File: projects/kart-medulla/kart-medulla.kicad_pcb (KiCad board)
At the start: 2 copper layers, 68 x 60 mm, 57 parts, among them CN1 1990012, CN2 1990012, CN3 1990012, CN4 1990012, CN5 1990012, CN6 1990012, CN7 1990012, CN8 1990012, Q3 IRLZ44NPBF, Q4 BSS123_C5184436, U1 LM358DR, U13 MCP4922-E/SL, U14 MAX4660EUA+T, U19 L7805CDT_C20611927, U23 SSW-122-01-T-D, U24 SSW-122-01-T-S, U25 PCF8574T/3,518, U5 SN74LVC3G17DCTR

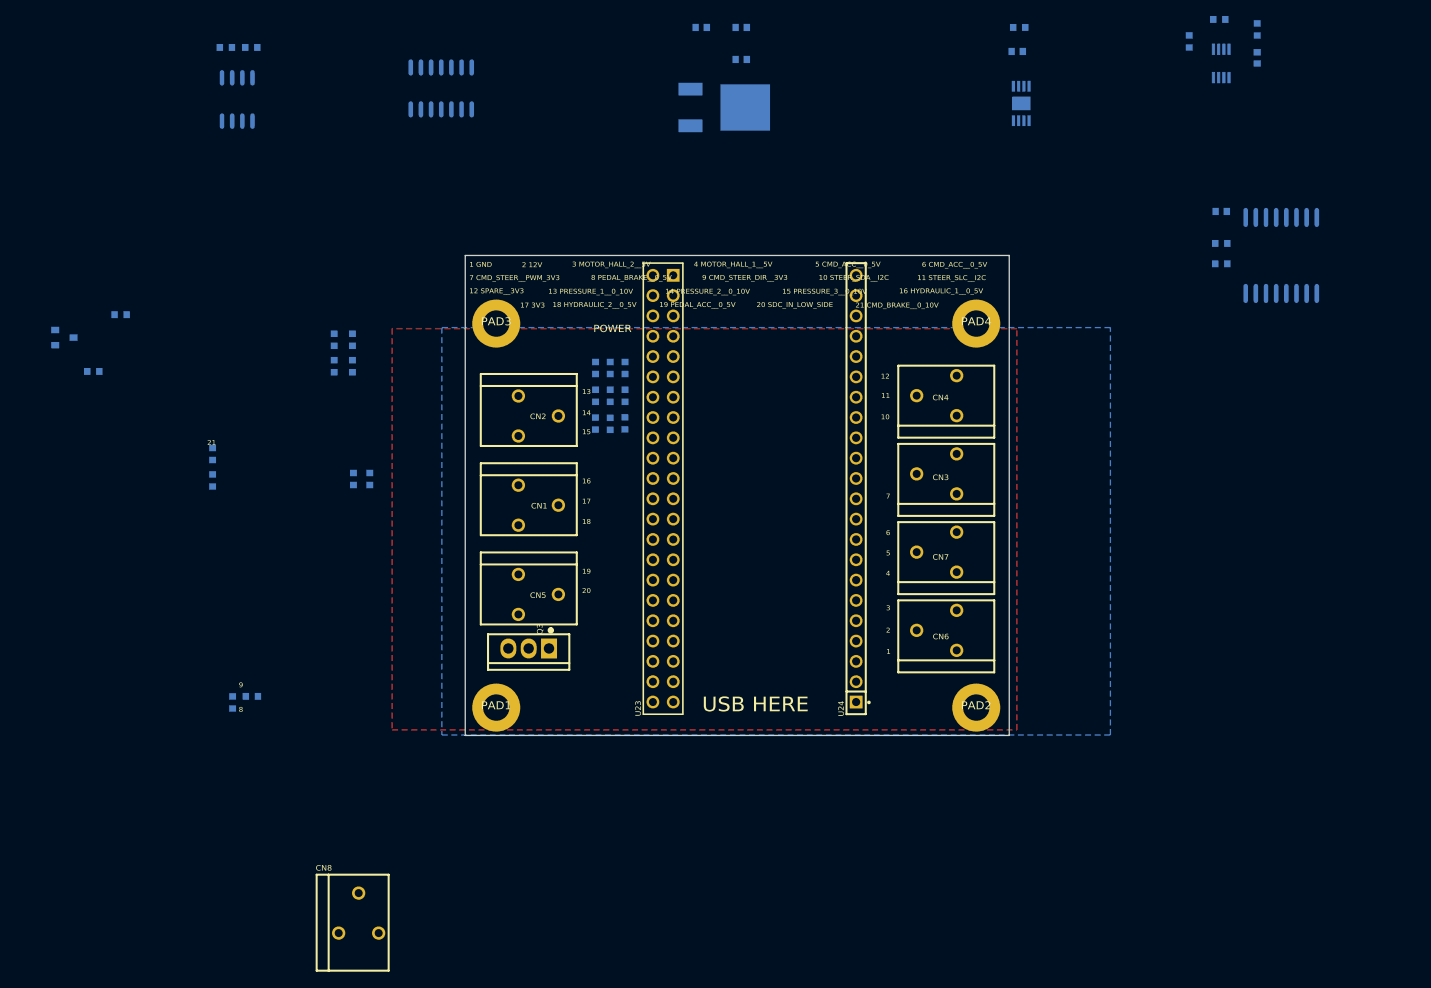
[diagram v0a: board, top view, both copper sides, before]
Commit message: kart-medulla: PCB↔schematic resync + agent workflow rules
PCB sync (the original goal — get ratsnest/Nets count right):
- Update PCB from Schematic with "Re-link footprints by reference"
  to repair empty symbol associations on every PCB footprint. Brings
  net count from 34 → ~80, ratsnest now populates correctly.
- Adds CN9, CN10 footprints that existed in schematic but not PCB.
- Footprint library names normalized to kart-medulla:* prefix.
- U23/U24 ESP32 header locks preserved (lock warnings benign).

Schematic cleanup:
- Delete stray kart-medulla:GND symbol with hidden Reference "U02"
  at (125.73, 311.15) — was buried under a standard power:GND at the
  same junction (redundant duplicate, no connectivity loss; ERC clean
  at that coord post-delete).

Agent workflow (addresses recurring failures in error-log):
- .agents/kicad-workflow.md — two-modes rule (read-only MCP vs
  direct-edit-with-KiCad-closed). KiCad has no schematic IPC API as
  of v10, so every schematic MCP server hand-rolls S-expression edits;
  mixing MCP writes with file edits silently clobbers. Default to
  Mode A (read-only MCP).
- scripts/guard-kicad-write.sh — pgrep preflight for KiCad GUI and
  kicad-mcp-pro before any agent-driven write.
- AGENTS.md — pointer to the workflow doc.
- .agents/kicad10-ui.md (user-authored) — verified UI cheat-sheet to
  stop the recurring "invented menu path" mistakes.
- tasks.md — buzzer circuit added to TODO.

Lessons logged in .agents/error-log.md and .agents/history.md:
- Don't grade edit options "safe vs risky" without grepping coords/nets first.
- Stacked symbols + Cmd+F selecting a Field-not-Symbol confusion in KiCad GUI.
- Don't pivot to unrelated TODOs while a workstream is in flight.
- kicad-sch-api round-trip is not format-preserving; not safe for writes.
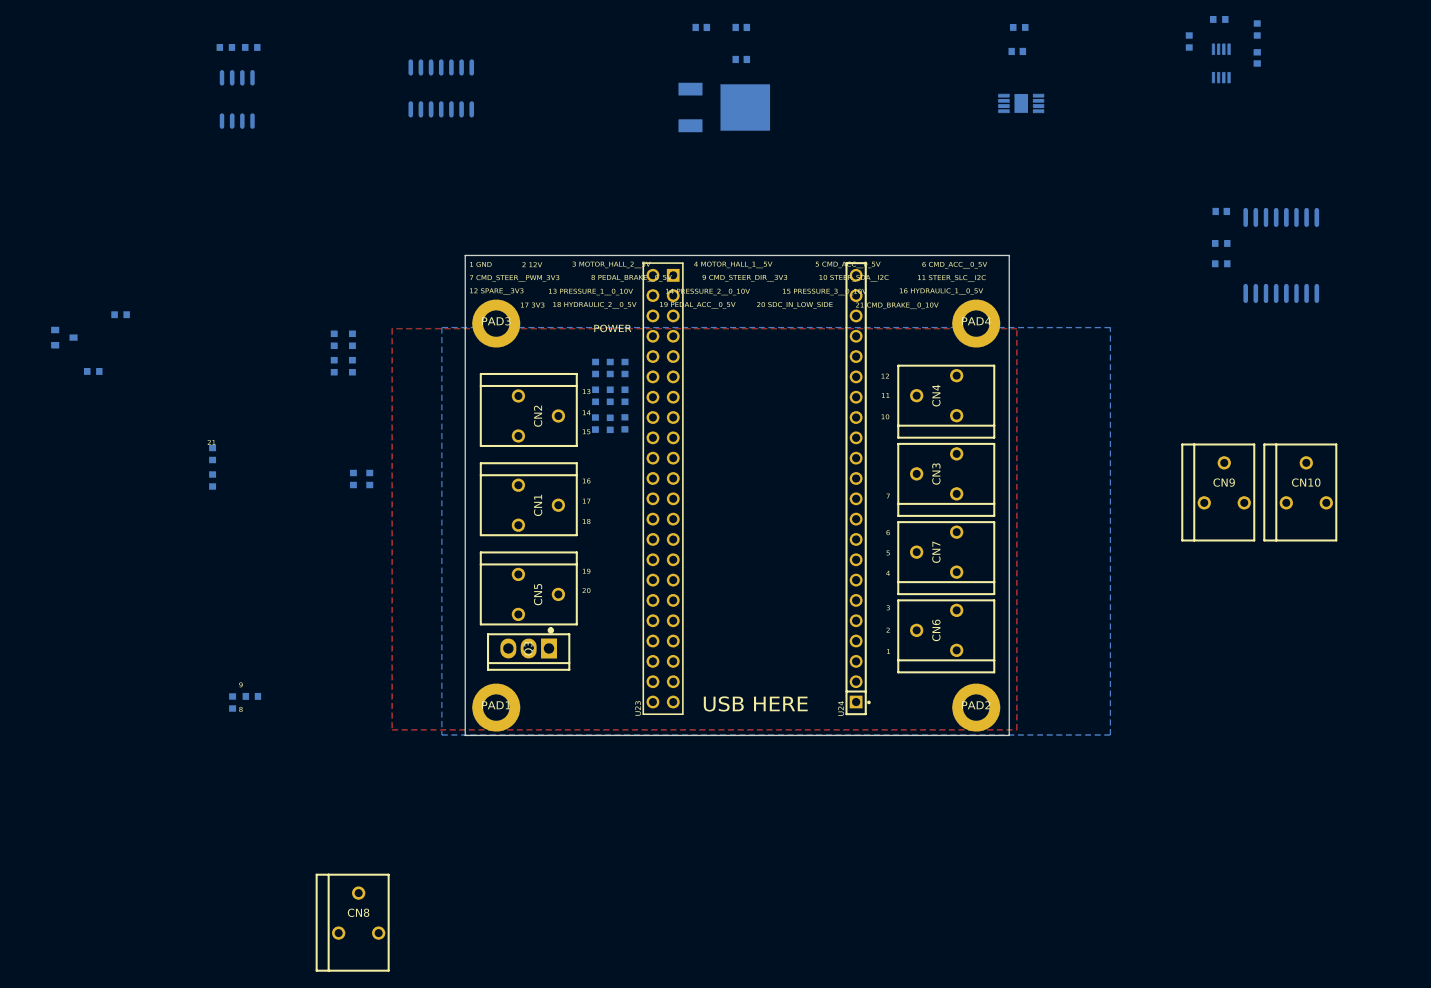
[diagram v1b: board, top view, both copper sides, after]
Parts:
- added CN10: 1990012, kart-medulla:CONN-TH_3P-P2.50-S5.00_1990012, F.Cu at (176.1, 72.4)
- added CN9: 1990012, kart-medulla:CONN-TH_3P-P2.50-S5.00_1990012, F.Cu at (165.9, 72.4)
- C1, C2, C3, C4, C5, C6: footprint C0603 -> kart-medulla:C0603
- CN1, CN2, CN3, CN4, CN5, CN6, CN7, CN8: footprint CONN-TH_3P-P2.50-S5.00_1990012 -> kart-medulla:CONN-TH_3P-P2.50-S5.00_1990012
- Q3: footprint TO-220-3_L10.0-W4.5-P2.54-T -> kart-medulla:TO-220-3_L10.0-W4.5-P2.54-T
- Q4: footprint SOT-23_L2.9-W1.3-P1.90-LS2.4-BR -> kart-medulla:SOT-23_L2.9-W1.3-P1.90-LS2.4-BR
- R1, R10, R11, R12, R13, R14, R15, R16, R17, R19, R2, R20, R22, R23, R24, R25, R26, R27, R3, R30, R31, R32, R33, R34, R4, R6, R7, R8, R9: footprint R0603 -> kart-medulla:R0603
- U13: footprint SOIC-14_L8.7-W3.9-P1.27-LS6.0-BL -> kart-medulla:SOIC-14_L8.7-W3.9-P1.27-LS6.0-BL
- U14: footprint UMAX-8_L3.0-W3.0-P0.65-LS4.9-BL-EP -> kart-medulla:SOP65P490X110-9N
- U19: footprint TO-252-2_L6.6-W6.1-P4.57-LS9.9-BR-CW -> kart-medulla:TO-252-2_L6.6-W6.1-P4.57-LS9.9-BR-CW
- U25: footprint SOIC-16_L10.3-W7.5-P1.27-LS10.3-BL -> kart-medulla:SOIC-16_L10.3-W7.5-P1.27-LS10.3-BL
- U5: footprint SOP65P400X130-8N -> kart-medulla:SOP65P400X130-8N
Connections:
- C1 pad 1: GND -> +3V3
- C1 pad 2: (no net) -> GND
- C2 pad 1: (no net) -> GND
- C2 pad 2: GND -> +12V
- C3 pad 1: (no net) -> GND
- C3 pad 2: GND -> +5V_REG
- C4 pad 1: (no net) -> GND
- C4 pad 2: GND -> +5V_REG
- C5 pad 1: (no net) -> GND
- C5 pad 2: GND -> +5V_REG
- C6 pad 2: (no net) -> +3V3
- CN1 pad 1: (no net) -> /P1/HYDRAULIC_1__0_5V
- CN1 pad 2: (no net) -> +3V3
- CN1 pad 3: (no net) -> /P1/HYDRAULIC_2__0_5V
- CN2 pad 1: (no net) -> /P1/PRESSURE_1__0_10V
- CN2 pad 2: (no net) -> /P1/PRESSURE_2__0_10V
- CN2 pad 3: (no net) -> /P1/PRESSURE_3__0_10V
- CN3 pad 1: (no net) -> /P1/CMD_STEER__PWM_3V3
- CN3 pad 2: (no net) -> /P1/PEDAL_BRAKE__0_5V
- CN3 pad 3: (no net) -> /P1/CMD_STEER_DIR__3V3
- CN4 pad 1: (no net) -> /P1/SDA__I2C
- CN4 pad 2: (no net) -> /P1/SCL__I2C
- CN4 pad 3: (no net) -> +3V3
- CN5 pad 1: (no net) -> /P1/PEDAL_ACC__0_5V
- CN5 pad 2: (no net) -> /P1/SDC_IN_LOW_SIDE
- CN5 pad 3: (no net) -> /P1/CMD_BRAKE__0_10V
- CN6 pad 2: (no net) -> +12V
- CN6 pad 3: (no net) -> /P1/MOTOR_HALL_2__5V
- CN7 pad 1: (no net) -> /P1/MOTOR_HALL_1__5V
- CN7 pad 2: (no net) -> /P1/MOTOR_HALL_3__5V
- CN7 pad 3: (no net) -> /P1/CMD_ACC__0_5V
- CN8 pad 1: (no net) -> /P1/REVERSE_WIRE
- CN8 pad 2: (no net) -> /P1/EXP_P2
- CN8 pad 3: (no net) -> /P1/EXP_P1
- Q3 pad 1: (no net) -> Net-(Q3-G)
- Q3 pad 2: (no net) -> /P1/SDC_IN_LOW_SIDE
- Q4 pad 1: (no net) -> Net-(Q4-G)
- Q4 pad 3: (no net) -> /P1/REVERSE_WIRE
- R1 pad 1: (no net) -> /P1/MOTOR_HALL_1__5V
- R1 pad 2: (no net) -> Net-(U5-1A)
- R10 pad 1: GND -> /P1/PRESSURE_3__0_3V3
- R10 pad 2: (no net) -> GND
- R11 pad 1: (no net) -> Net-(R11-Pad1)
- R11 pad 2: (no net) -> /P1/PRESSURE_1__0_10V
- R12 pad 1: (no net) -> Net-(R11-Pad1)
- R12 pad 2: (no net) -> /P1/PRESSURE_1__0_3V3
- R13 pad 1: GND -> /P1/PRESSURE_1__0_3V3
- R13 pad 2: (no net) -> GND
- R14 pad 1: (no net) -> /P1/PEDAL_ACC__3V3
- R14 pad 2: (no net) -> /P1/PEDAL_ACC__0_5V
- R15 pad 1: GND -> /P1/PEDAL_ACC__3V3
- R15 pad 2: (no net) -> GND
- R16 pad 1: (no net) -> /P1/PEDAL_BRAKE__3V3
- R16 pad 2: (no net) -> /P1/PEDAL_BRAKE__0_5V
- R17 pad 1: GND -> /P1/PEDAL_BRAKE__3V3
- R17 pad 2: (no net) -> GND
- R19 pad 1: (no net) -> Net-(U1A--IN1)
- R19 pad 2: (no net) -> /P1/CMD_BRAKE__0_10V
- R2 pad 1: (no net) -> /P1/MOTOR_HALL_2__5V
- R2 pad 2: (no net) -> Net-(U5-2A)
- R20 pad 2: (no net) -> Net-(U1A--IN1)
- R22 pad 1: (no net) -> Net-(Q3-G)
- R22 pad 2: (no net) -> /P1/SDC_NOT_EMERGENCY__3V3
- R23 pad 2: (no net) -> Net-(Q3-G)
- R24 pad 1: (no net) -> /P1/HYDRAULIC_1__0_3V3
- R24 pad 2: (no net) -> /P1/HYDRAULIC_1__0_5V
- R25 pad 1: GND -> /P1/HYDRAULIC_1__0_3V3
- R25 pad 2: (no net) -> GND
- R26 pad 1: (no net) -> /P1/HYDRAULIC_2__0_3V3
- R26 pad 2: (no net) -> /P1/HYDRAULIC_2__0_5V
- R27 pad 1: GND -> /P1/HYDRAULIC_2__0_3V3
- R27 pad 2: (no net) -> GND
- R3 pad 1: (no net) -> /P1/MOTOR_HALL_3__5V
- R3 pad 2: (no net) -> Net-(U5-3A)
- R30 pad 1: (no net) -> /P1/CMD_REVERSE
- R30 pad 2: (no net) -> Net-(Q4-G)
- R31 pad 1: GND -> Net-(Q4-G)
- R31 pad 2: (no net) -> GND
- R32 pad 1: GND -> /P1/SELECT_THROTTLE
- R32 pad 2: (no net) -> GND
- R33 pad 1: (no net) -> /P1/SDA__I2C
- R33 pad 2: (no net) -> +3V3
- R34 pad 1: (no net) -> /P1/SCL__I2C
- R34 pad 2: (no net) -> +3V3
- R4 pad 1: (no net) -> Net-(R4-Pad1)
- R4 pad 2: (no net) -> /P1/PRESSURE_2__0_10V
- R6 pad 1: (no net) -> Net-(R4-Pad1)
- R6 pad 2: (no net) -> /P1/PRESSURE_2__0_3V3
- R7 pad 1: GND -> /P1/PRESSURE_2__0_3V3
- R7 pad 2: (no net) -> GND
- R8 pad 1: (no net) -> Net-(R8-Pad1)
- R8 pad 2: (no net) -> /P1/PRESSURE_3__0_10V
- R9 pad 1: (no net) -> Net-(R8-Pad1)
- R9 pad 2: (no net) -> /P1/PRESSURE_3__0_3V3
- U1 pad 1: (no net) -> /P1/CMD_BRAKE__0_10V
- U1 pad 2: (no net) -> Net-(U1A--IN1)
- U1 pad 3: (no net) -> /P1/CMD_BRAKE__0_5V
- U1 pad 5: (no net) -> GND
- U1 pad 6: (no net) -> Net-(U1B--IN2)
- U1 pad 7: (no net) -> Net-(U1B--IN2)
- U1 pad 8: (no net) -> +12V
- U13 pad 1: (no net) -> +5V_REG
- U13 pad 10: (no net) -> /P1/CMD_BRAKE__0_5V
- U13 pad 11: (no net) -> +5V_REG
- U13 pad 13: (no net) -> +5V_REG
- U13 pad 14: (no net) -> /P1/CMD_ACC_ESP32__0_5V
- U13 pad 2: (no net) -> unconnected-(U13-NC-Pad2)
- U13 pad 3: (no net) -> /P1/CMD_DAC_CS
- U13 pad 4: (no net) -> /P1/CLK
- U13 pad 5: (no net) -> /P1/MOSI
- U13 pad 6: (no net) -> unconnected-(U13-NC-Pad6)
- U13 pad 7: (no net) -> unconnected-(U13-NC-Pad7)
- U13 pad 9: (no net) -> +5V_REG
- U14 pad 1: (no net) -> /P1/CMD_ACC__0_5V
- U14 pad 2: (no net) -> /P1/PEDAL_ACC__0_5V
- U14 pad 4: (no net) -> +5V_REG
- U14 pad 5: (no net) -> unconnected-(U14-NC-Pad5)
- U14 pad 6: (no net) -> /P1/SELECT_THROTTLE
- U14 pad 8: (no net) -> /P1/CMD_ACC_ESP32__0_5V
- U19 pad 1: (no net) -> +12V
- U19 pad 3: (no net) -> +5V_REG
- U23 pad 1: (no net) -> +3V3
- U23 pad 10: (no net) -> /P1/PEDAL_BRAKE__3V3
- U23 pad 11: (no net) -> /P1/PRESSURE_1__0_3V3
- U23 pad 12: (no net) -> /P1/PRESSURE_1__0_3V3
- U23 pad 13: (no net) -> /P1/PRESSURE_2__0_3V3
- U23 pad 14: (no net) -> /P1/PRESSURE_2__0_3V3
- U23 pad 15: (no net) -> /P1/SELECT_THROTTLE
- U23 pad 16: (no net) -> /P1/SELECT_THROTTLE
- U23 pad 17: (no net) -> /P1/MOTOR_HALL_1__3V3
- U23 pad 18: (no net) -> /P1/MOTOR_HALL_1__3V3
- U23 pad 19: (no net) -> unconnected-(U23-Pad19)
- U23 pad 2: (no net) -> +3V3
- U23 pad 20: (no net) -> unconnected-(U23-Pad20)
- U23 pad 21: (no net) -> unconnected-(U23-Pad21)
- U23 pad 22: (no net) -> unconnected-(U23-Pad22)
- U23 pad 23: (no net) -> /P1/SDA__I2C
- U23 pad 24: (no net) -> /P1/SDA__I2C
- U23 pad 25: (no net) -> /P1/BUZZER
- U23 pad 26: (no net) -> /P1/BUZZER
- U23 pad 27: (no net) -> unconnected-(U23-Pad27)
- U23 pad 28: (no net) -> unconnected-(U23-Pad28)
- U23 pad 29: (no net) -> /P1/SCL__I2C
- U23 pad 3: (no net) -> +3V3
- U23 pad 30: (no net) -> /P1/SCL__I2C
- U23 pad 31: (no net) -> /P1/HYDRAULIC_1__0_3V3
- U23 pad 32: (no net) -> /P1/HYDRAULIC_1__0_3V3
- U23 pad 33: (no net) -> /P1/MOSI
- U23 pad 34: (no net) -> /P1/MOSI
- U23 pad 35: (no net) -> /P1/CLK
- U23 pad 36: (no net) -> /P1/CLK
- U23 pad 37: (no net) -> /P1/MISO
- U23 pad 38: (no net) -> /P1/MISO
- U23 pad 39: (no net) -> /P1/CMD_DAC_CS
- U23 pad 4: (no net) -> +3V3
- U23 pad 40: (no net) -> /P1/CMD_DAC_CS
- U23 pad 41: (no net) -> +5V_USB
- U23 pad 42: (no net) -> +5V_USB
- U23 pad 43: (no net) -> GND
- U23 pad 44: (no net) -> GND
- U23 pad 5: (no net) -> /P1/RESET
- U23 pad 6: (no net) -> /P1/RESET
- U23 pad 7: (no net) -> /P1/PEDAL_ACC__3V3
- U23 pad 8: (no net) -> /P1/PEDAL_ACC__3V3
- U23 pad 9: (no net) -> /P1/PEDAL_BRAKE__3V3
- U24 pad 1: (no net) -> GND
- U24 pad 10: (no net) -> unconnected-(U24-Pad10)
- U24 pad 11: (no net) -> unconnected-(U24-Pad11)
- U24 pad 12: (no net) -> unconnected-(U24-Pad12)
- U24 pad 13: (no net) -> /P1/SDC_NOT_EMERGENCY__3V3
- U24 pad 14: (no net) -> unconnected-(U24-Pad14)
- U24 pad 15: (no net) -> /P1/CMD_STEER__PWM_3V3
- U24 pad 16: (no net) -> unconnected-(U24-Pad16)
- U24 pad 17: (no net) -> unconnected-(U24-Pad17)
- U24 pad 18: (no net) -> /P1/HYDRAULIC_2__0_3V3
- U24 pad 19: (no net) -> /P1/PRESSURE_3__0_3V3
- U24 pad 2: (no net) -> GND
- U24 pad 20: (no net) -> unconnected-(U24-Pad20)
- U24 pad 21: (no net) -> unconnected-(U24-Pad21)
- U24 pad 22: (no net) -> GND
- U24 pad 3: (no net) -> unconnected-(U24-Pad3)
- U24 pad 4: (no net) -> unconnected-(U24-Pad4)
- U24 pad 5: (no net) -> /P1/MOTOR_HALL_3__3V3
- U24 pad 6: (no net) -> /P1/MOTOR_HALL_2__3V3
- U24 pad 7: (no net) -> unconnected-(U24-Pad7)
- U24 pad 8: (no net) -> unconnected-(U24-Pad8)
- U24 pad 9: (no net) -> /P1/CMD_STEER_DIR__3V3
- U25 pad 10: (no net) -> /P1/EXP_P5
- U25 pad 11: (no net) -> /P1/EXP_P6
- U25 pad 12: (no net) -> /P1/EXP_P7
- U25 pad 13: (no net) -> unconnected-(U25-INT#-Pad13)
- U25 pad 14: (no net) -> /P1/SCL__I2C
- U25 pad 15: (no net) -> /P1/SDA__I2C
- U25 pad 16: (no net) -> +3V3
- U25 pad 4: (no net) -> /P1/CMD_REVERSE
- U25 pad 5: (no net) -> /P1/EXP_P1
- U25 pad 6: (no net) -> /P1/EXP_P2
- U25 pad 7: (no net) -> /P1/EXP_P3
- U25 pad 9: (no net) -> /P1/EXP_P4
- U5 pad 1: (no net) -> Net-(U5-1A)
- U5 pad 2: (no net) -> /P1/MOTOR_HALL_3__3V3
- U5 pad 3: (no net) -> Net-(U5-2A)
- U5 pad 5: (no net) -> /P1/MOTOR_HALL_2__3V3
- U5 pad 6: (no net) -> Net-(U5-3A)
- U5 pad 7: (no net) -> /P1/MOTOR_HALL_1__3V3
- U5 pad 8: (no net) -> +3V3

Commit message: Fix duplicate signal mess
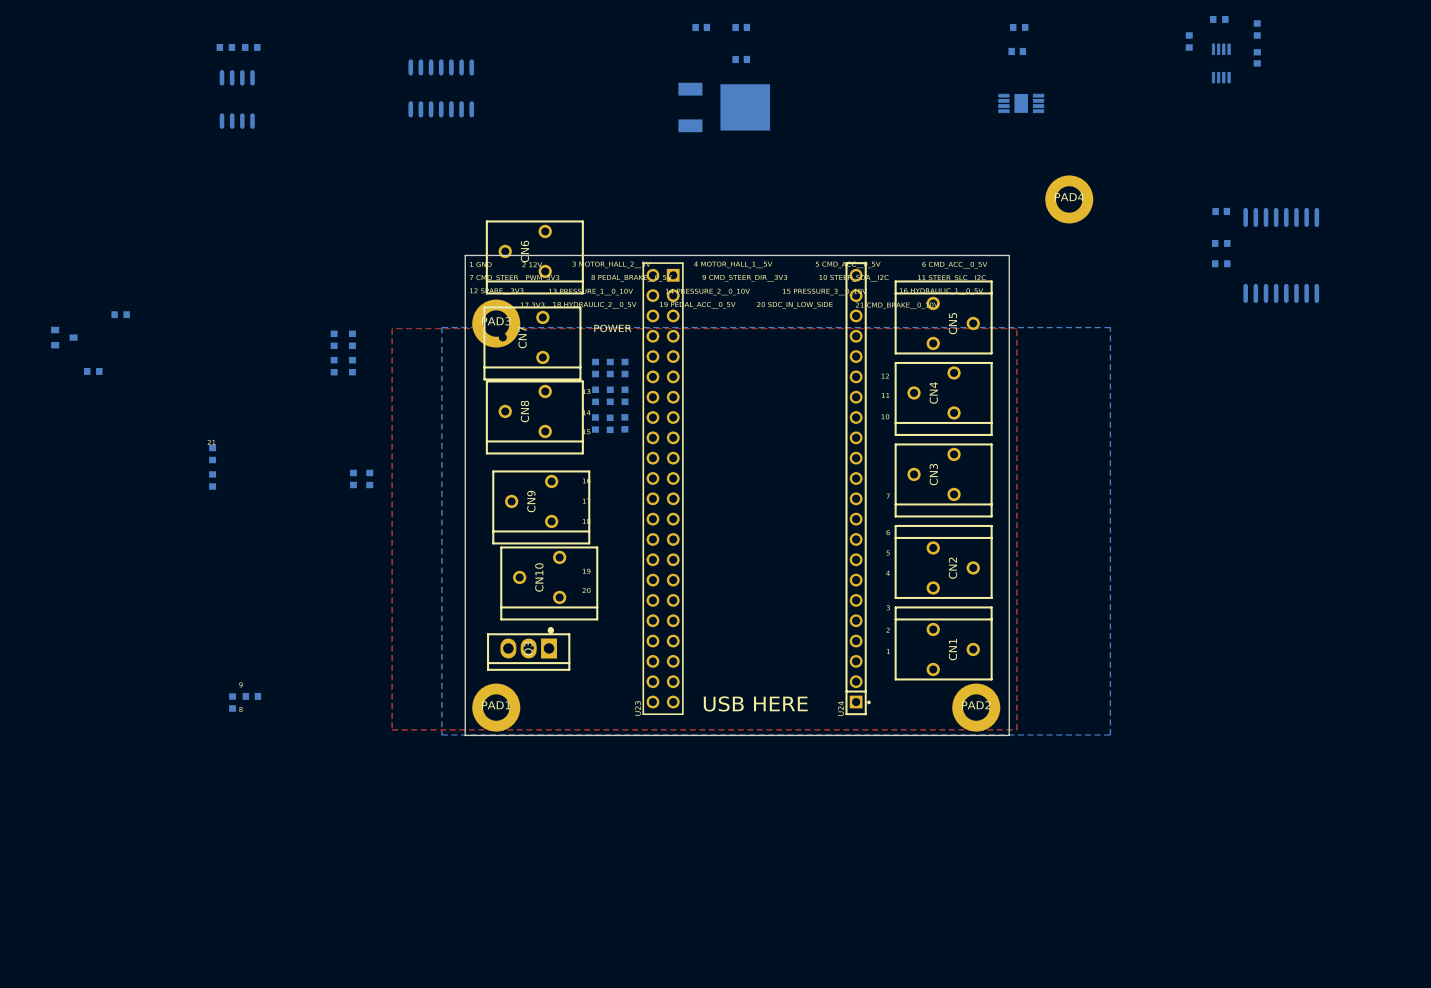
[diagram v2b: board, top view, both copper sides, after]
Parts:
- moved CN10 96.6 mm to (80.3, 84.2), turned to 90 degrees
- moved CN9 86.6 mm to (79.3, 74.8), turned to 90 degrees
- moved CN6 69.9 mm to (78.5, 43.5)
- moved CN8 66.1 mm to (78.5, 63.5), turned to 90 degrees
- moved CN5 61.9 mm to (132.0, 52.5)
- moved CN7 58.3 mm to (78.2, 54.2)
- moved CN2 55.2 mm to (132.0, 83.1)
- moved CN1 54.9 mm to (132.0, 93.2)
- moved PAD4 19.4 mm to (146.5, 37.0)
- moved CN4 0.47 mm to (129.6, 61.2)
- moved CN3 0.33 mm to (129.6, 71.4)

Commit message: pcb ok
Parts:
- U23: footprint HDR-TH_ESQ-122-59-G-D -> kart-medulla:HDR-TH_ESQ-122-59-G-D
- U24: footprint HDR-TH_ESQ-122-23-G-S -> kart-medulla:HDR-TH_ESQ-122-23-G-S
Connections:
- CN1 pad 1: /P1/HYDRAULIC_1__0_5V -> GND
- CN1 pad 2: +3V3 -> +12V
- CN1 pad 3: /P1/HYDRAULIC_2__0_5V -> GND
- CN10 pad 1: GND -> /P1/CMD_ACC__0_5V
- CN10 pad 2: /P1/EXP_P7 -> /P1/CMD_BRAKE__0_5V
- CN10 pad 3: /P1/EXP_P6 -> GND
- CN2 pad 1: /P1/PRESSURE_1__0_10V -> /P1/MOTOR_HALL_3__5V
- CN2 pad 2: /P1/PRESSURE_2__0_10V -> /P1/MOTOR_HALL_2__5V
- CN2 pad 3: /P1/PRESSURE_3__0_10V -> +5V_REG
- CN3 pad 1: /P1/CMD_STEER__PWM_3V3 -> /P1/CMD_STEER_DIR__3V3
- CN3 pad 2: /P1/PEDAL_BRAKE__0_5V -> /P1/EXP_P1
- CN3 pad 3: /P1/CMD_STEER_DIR__3V3 -> /P1/EXP_P2
- CN4 pad 1: /P1/SDA__I2C -> /P1/REVERSE_WIRE
- CN4 pad 2: /P1/SCL__I2C -> /P1/SDC_IN_LOW_SIDE
- CN4 pad 3: +3V3 -> /P1/CMD_STEER__PWM_3V3
- CN5 pad 1: /P1/PEDAL_ACC__0_5V -> /P1/HYDRAULIC_2__0_5V
- CN5 pad 2: /P1/SDC_IN_LOW_SIDE -> /P1/PRESSURE_3__0_10V
- CN5 pad 3: /P1/CMD_BRAKE__0_10V -> GND
- CN6 pad 1: GND -> /P1/PEDAL_ACC__0_5V
- CN6 pad 2: +12V -> /P1/PEDAL_BRAKE__0_5V
- CN6 pad 3: /P1/MOTOR_HALL_2__5V -> +3V3
- CN7 pad 1: /P1/MOTOR_HALL_1__5V -> /P1/PRESSURE_1__0_10V
- CN7 pad 2: /P1/MOTOR_HALL_3__5V -> /P1/PRESSURE_2__0_10V
- CN7 pad 3: /P1/CMD_ACC__0_5V -> /P1/MOTOR_HALL_1__5V
- CN8 pad 1: /P1/REVERSE_WIRE -> /P1/SDA__I2C
- CN8 pad 2: /P1/EXP_P2 -> /P1/BUZZER
- CN8 pad 3: /P1/EXP_P1 -> /P1/EXP_P3
- CN9 pad 1: /P1/EXP_P5 -> /P1/SCL__I2C
- CN9 pad 2: /P1/EXP_P4 -> /P1/HYDRAULIC_1__0_5V
- CN9 pad 3: /P1/EXP_P3 -> /P1/EXP_P4
- U25 pad 10: /P1/EXP_P5 -> unconnected-(U25-P5-Pad10)
- U25 pad 11: /P1/EXP_P6 -> unconnected-(U25-P6-Pad11)
- U25 pad 12: /P1/EXP_P7 -> unconnected-(U25-P7-Pad12)

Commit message: pcb until nets update
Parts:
- moved R11 81.1 mm to (18.5, 101.0)
- moved R12 81.1 mm to (20.3, 101.0)
- moved R4 81.1 mm to (18.5, 104.5)
- moved R6 81.1 mm to (20.3, 104.5)
- moved R8 81.1 mm to (18.5, 108.0)
- moved R9 81.1 mm to (20.3, 108.0)
- moved R10 81.1 mm to (22.2, 107.9)
- moved R13 81.1 mm to (22.2, 101.0)
- moved R7 81.1 mm to (22.2, 104.5)
- moved R26 69.2 mm to (18.8, 117.0)
- moved R27 69.2 mm to (21.1, 117.0)
- moved R24 69.2 mm to (18.8, 113.7)
- moved R25 69.2 mm to (21.1, 113.7)
- moved R14 63.4 mm to (20.4, 122.2)
- moved R15 63.4 mm to (18.3, 122.2)
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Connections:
- CN3 pad 1: /P1/CMD_STEER_DIR__3V3 -> /P1/EXP_P3
- CN4 pad 2: /P1/SDC_IN_LOW_SIDE -> /P1/SDA__I2C
- CN4 pad 3: /P1/CMD_STEER__PWM_3V3 -> /P1/SCL__I2C
- CN8 pad 1: /P1/SDA__I2C -> /P1/SDC_IN_LOW_SIDE
- CN8 pad 3: /P1/EXP_P3 -> /P1/CMD_STEER_DIR__3V3
- CN9 pad 1: /P1/SCL__I2C -> /P1/CMD_STEER__PWM_3V3
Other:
- board size 68 x 60 mm -> 68.9 x 66.5 mm
- board text removed: "1 GND"
- board text removed: "10 STEER_SDA__I2C"
- board text removed: "11 STEER_SLC__I2C"
- board text removed: "12 SPARE__3V3"
- board text removed: "13 PRESSURE_1__0_10V"
- board text removed: "14 PRESSURE_2__0_10V"
- board text removed: "15 PRESSURE_3__0_10V"
- board text removed: "16 HYDRAULIC_1__0_5V"
- board text removed: "18 HYDRAULIC_2__0_5V"
- board text removed: "19 PEDAL_ACC__0_5V"
- board text removed: "2 12V"
- board text removed: "20 SDC_IN_LOW_SIDE"
- board text removed: "21 CMD_BRAKE__0_10V"
- board text removed: "3 MOTOR_HALL_2__5V"
- board text removed: "4 MOTOR_HALL_1__5V"
- board text removed: "5 CMD_ACC__0_5V"
- board text removed: "6 CMD_ACC__0_5V"
- board text removed: "7 CMD_STEER__PWM_3V3"
- board text removed: "8 PEDAL_BRAKE__0_5V"
- board text removed: "9 CMD_STEER_DIR__3V3"
